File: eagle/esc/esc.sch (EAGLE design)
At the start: 88 parts, among them IC1 DRV8305NPHPR, IC2 STM32L431CCT6LQFP48, IC3 FT232RL, J2 ARM10-CON, T1 CSD17573Q5B, T2 CSD17573Q5B, T3 CSD17573Q5B, T4 CSD17573Q5B, T5 CSD17573Q5B, T6 CSD17573Q5B, U1 LD1117S50TR1, U2 MIC5319-3.3YD5-TR, X1 C-GRID-02-15-19, X2 MINI-USB-32005-301

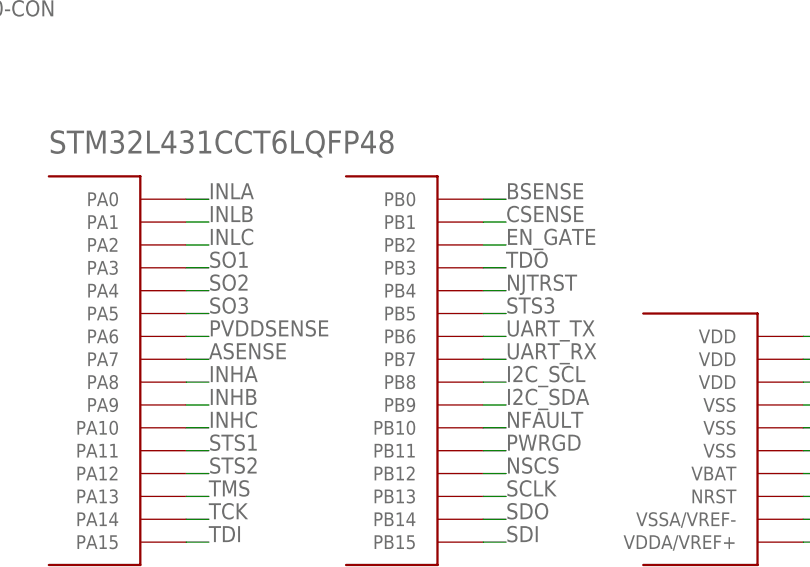
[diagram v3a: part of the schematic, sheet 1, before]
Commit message: updated pin mappings - changed a bunch for better placements
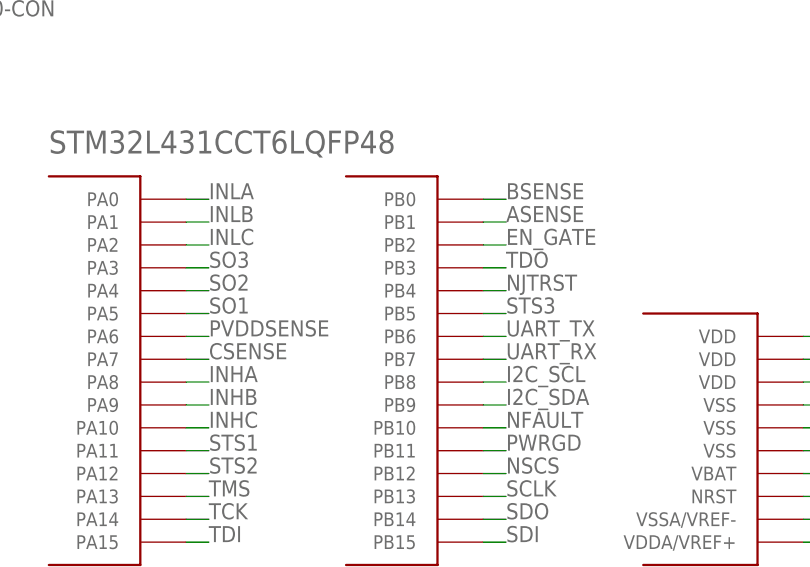
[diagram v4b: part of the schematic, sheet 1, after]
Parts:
- C2, C5, C8: device resistor:C-EUC0603 -> resistor:C-EUC0402
- R1, R2, R4, R5, R7, R8: device resistor:R-US_R0603 -> resistor:R-US_R0402
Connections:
- net ASENSE: now also IC2.PB1; no longer IC2.PA7
- net CSENSE: now also IC2.PA7; no longer IC2.PB1
- net SO1: now also IC2.PA5; no longer IC2.PA3
- net SO3: now also IC2.PA3; no longer IC2.PA5
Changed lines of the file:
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@@
 <part name="IC2" library="qc_esc" deviceset="STM32L431CCT6" device="LQFP48" package3d_urn="urn:adsk.eagle:package:16300078/1"/>
 <part name="C1" library="resistor" library_urn="urn:adsk.eagle:library:348" deviceset="C-EU" device="C0603" package3d_urn="urn:adsk.eagle:package:23616/2" value="1 uF"/>
-<part name="C2" library="resistor" library_urn="urn:adsk.eagle:library:348" deviceset="C-EU" device="C0603" package3d_urn="urn:adsk.eagle:package:23616/2" value="0.1 uF"/>
+<part name="C2" library="resistor" library_urn="urn:adsk.eagle:library:348" deviceset="C-EU" device="C0402" package3d_urn="urn:adsk.eagle:package:23626/2" value="0.1 uF"/>
 <part name="D1" library="qc_esc" deviceset="STPS2L30A" device="SMA" package3d_urn="urn:adsk.eagle:package:18881571/1"/>
-<part name="R1" library="resistor" library_urn="urn:adsk.eagle:library:348" deviceset="R-US_" device="R0603" package3d_urn="urn:adsk.eagle:package:23555/3" value="34.8k"/>
-<part name="R2" library="resistor" library_urn="urn:adsk.eagle:library:348" deviceset="R-US_" device="R0603" package3d_urn="urn:adsk.eagle:package:23555/3" value="4.99k"/>
+<part name="R1" library="resistor" library_urn="urn:adsk.eagle:library:348" deviceset="R-US_" device="R0402" package3d_urn="urn:adsk.eagle:package:26058/2" value="34.8k"/>
+<part name="R2" library="resistor" library_urn="urn:adsk.eagle:library:348" deviceset="R-US_" device="R0402" package3d_urn="urn:adsk.eagle:package:26058/2" value="4.99k"/>
 <part name="VDD1" library="supply1" library_urn="urn:adsk.eagle:library:371" deviceset="VDD" device=""/>
 <part name="SUPPLY1" library="supply2" library_urn="urn:adsk.eagle:library:372" deviceset="GND" device=""/>
@@
 <part name="T4" library="qc_esc" deviceset="CSD17573Q5B" device=""/>
 <part name="C4" library="resistor" library_urn="urn:adsk.eagle:library:348" deviceset="C-EU" device="C0603" package3d_urn="urn:adsk.eagle:package:23616/2" value="1 uF"/>
-<part name="C5" library="resistor" library_urn="urn:adsk.eagle:library:348" deviceset="C-EU" device="C0603" package3d_urn="urn:adsk.eagle:package:23616/2" value="0.1 uF"/>
+<part name="C5" library="resistor" library_urn="urn:adsk.eagle:library:348" deviceset="C-EU" device="C0402" package3d_urn="urn:adsk.eagle:package:23626/2" value="0.1 uF"/>
 <part name="D2" library="qc_esc" deviceset="STPS2L30A" device="SMA" package3d_urn="urn:adsk.eagle:package:18881571/1"/>
-<part name="R4" library="resistor" library_urn="urn:adsk.eagle:library:348" deviceset="R-US_" device="R0603" package3d_urn="urn:adsk.eagle:package:23555/3" value="34.8k"/>
-<part name="R5" library="resistor" library_urn="urn:adsk.eagle:library:348" deviceset="R-US_" device="R0603" package3d_urn="urn:adsk.eagle:package:23555/3" value="4.99k"/>
+<part name="R4" library="resistor" library_urn="urn:adsk.eagle:library:348" deviceset="R-US_" device="R0402" package3d_urn="urn:adsk.eagle:package:26058/2" value="34.8k"/>
+<part name="R5" library="resistor" library_urn="urn:adsk.eagle:library:348" deviceset="R-US_" device="R0402" package3d_urn="urn:adsk.eagle:package:26058/2" value="4.99k"/>
 <part name="VDD2" library="supply1" library_urn="urn:adsk.eagle:library:371" deviceset="VDD" device=""/>
 <part name="SUPPLY4" library="supply2" library_urn="urn:adsk.eagle:library:372" deviceset="GND" device=""/>
@@
 <part name="T6" library="qc_esc" deviceset="CSD17573Q5B" device=""/>
 <part name="C7" library="resistor" library_urn="urn:adsk.eagle:library:348" deviceset="C-EU" device="C0603" package3d_urn="urn:adsk.eagle:package:23616/2" value="1 uF"/>
-<part name="C8" library="resistor" library_urn="urn:adsk.eagle:library:348" deviceset="C-EU" device="C0603" package3d_urn="urn:adsk.eagle:package:23616/2" value="0.1 uF"/>
+<part name="C8" library="resistor" library_urn="urn:adsk.eagle:library:348" deviceset="C-EU" device="C0402" package3d_urn="urn:adsk.eagle:package:23626/2" value="0.1 uF"/>
 <part name="D3" library="qc_esc" deviceset="STPS2L30A" device="SMA" package3d_urn="urn:adsk.eagle:package:18881571/1"/>
-<part name="R7" library="resistor" library_urn="urn:adsk.eagle:library:348" deviceset="R-US_" device="R0603" package3d_urn="urn:adsk.eagle:package:23555/3" value="34.8k"/>
-<part name="R8" library="resistor" library_urn="urn:adsk.eagle:library:348" deviceset="R-US_" device="R0603" package3d_urn="urn:adsk.eagle:package:23555/3" value="4.99k"/>
+<part name="R7" library="resistor" library_urn="urn:adsk.eagle:library:348" deviceset="R-US_" device="R0402" package3d_urn="urn:adsk.eagle:package:26058/2" value="34.8k"/>
+<part name="R8" library="resistor" library_urn="urn:adsk.eagle:library:348" deviceset="R-US_" device="R0402" package3d_urn="urn:adsk.eagle:package:26058/2" value="4.99k"/>
 <part name="VDD3" library="supply1" library_urn="urn:adsk.eagle:library:371" deviceset="VDD" device=""/>
 <part name="SUPPLY7" library="supply2" library_urn="urn:adsk.eagle:library:372" deviceset="GND" device=""/>
@@
 <net name="SO1" class="0">
 <segment>
-<pinref part="IC2" gate="G$1" pin="PA3"/>
-<wire x1="66.04" y1="91.44" x2="68.58" y2="91.44" width="0.1524" layer="91"/>
-<label x="68.58" y="91.44" size="1.778" layer="95"/>
+<pinref part="IC2" gate="G$1" pin="PA5"/>
+<wire x1="66.04" y1="86.36" x2="68.58" y2="86.36" width="0.1524" layer="91"/>
+<label x="68.58" y="86.36" size="1.778" layer="95"/>
 </segment>
 </net>
@@
 </segment>
 </net>
-<net name="SO3" class="0">
-<segment>
-<pinref part="IC2" gate="G$1" pin="PA5"/>
-<wire x1="66.04" y1="86.36" x2="68.58" y2="86.36" width="0.1524" layer="91"/>
-<label x="68.58" y="86.36" size="1.778" layer="95"/>
-</segment>
-</net>
 <net name="PVDDSENSE" class="0">
 <segment>
@@
 </segment>
 </net>
-<net name="ASENSE" class="0">
+<net name="INHA" class="0">
+<segment>
+<pinref part="IC2" gate="G$1" pin="PA8"/>
+<wire x1="66.04" y1="78.74" x2="68.58" y2="78.74" width="0.1524" layer="91"/>
+<label x="68.58" y="78.74" size="1.778" layer="95"/>
+</segment>
+</net>
+<net name="INHB" class="0">
+<segment>
+<pinref part="IC2" gate="G$1" pin="PA9"/>
+<wire x1="66.04" y1="76.2" x2="68.58" y2="76.2" width="0.1524" layer="91"/>
+<label x="68.58" y="76.2" size="1.778" layer="95"/>
+</segment>
+</net>
+<net name="INHC" class="0">
+<segment>
+<pinref part="IC2" gate="G$1" pin="PA10"/>
+<wire x1="66.04" y1="73.66" x2="68.58" y2="73.66" width="0.1524" layer="91"/>
+<label x="68.58" y="73.66" size="1.778" layer="95"/>
+</segment>
+</net>
+<net name="BSENSE" class="0">
+<segment>
+<pinref part="IC2" gate="G$1" pin="PB0"/>
+<wire x1="99.06" y1="99.06" x2="101.6" y2="99.06" width="0.1524" layer="91"/>
+<label x="101.6" y="99.06" size="1.778" layer="95"/>
+</segment>
+</net>
+<net name="CSENSE" class="0">
 <segment>
 <pinref part="IC2" gate="G$1" pin="PA7"/>
 <wire x1="66.04" y1="81.28" x2="68.58" y2="81.28" width="0.1524" layer="91"/>
 <label x="68.58" y="81.28" size="1.778" layer="95"/>
-</segment>
-</net>
-<net name="INHA" class="0">
-<segment>
-<pinref part="IC2" gate="G$1" pin="PA8"/>
-<wire x1="66.04" y1="78.74" x2="68.58" y2="78.74" width="0.1524" layer="91"/>
-<label x="68.58" y="78.74" size="1.778" layer="95"/>
-</segment>
-</net>
-<net name="INHB" class="0">
-<segment>
-<pinref part="IC2" gate="G$1" pin="PA9"/>
-<wire x1="66.04" y1="76.2" x2="68.58" y2="76.2" width="0.1524" layer="91"/>
-<label x="68.58" y="76.2" size="1.778" layer="95"/>
-</segment>
-</net>
-<net name="INHC" class="0">
-<segment>
-<pinref part="IC2" gate="G$1" pin="PA10"/>
-<wire x1="66.04" y1="73.66" x2="68.58" y2="73.66" width="0.1524" layer="91"/>
-<label x="68.58" y="73.66" size="1.778" layer="95"/>
-</segment>
-</net>
-<net name="BSENSE" class="0">
-<segment>
-<pinref part="IC2" gate="G$1" pin="PB0"/>
-<wire x1="99.06" y1="99.06" x2="101.6" y2="99.06" width="0.1524" layer="91"/>
-<label x="101.6" y="99.06" size="1.778" layer="95"/>
-</segment>
-</net>
-<net name="CSENSE" class="0">
-<segment>
-<pinref part="IC2" gate="G$1" pin="PB1"/>
-<wire x1="99.06" y1="96.52" x2="101.6" y2="96.52" width="0.1524" layer="91"/>
-<label x="101.6" y="96.52" size="1.778" layer="95"/>
 </segment>
 </net>
@@
 </segment>
 </net>
+<net name="SO3" class="0">
+<segment>
+<pinref part="IC2" gate="G$1" pin="PA3"/>
+<wire x1="66.04" y1="91.44" x2="68.58" y2="91.44" width="0.1524" layer="91"/>
+<label x="68.58" y="91.44" size="1.778" layer="95"/>
+</segment>
+</net>
+<net name="ASENSE" class="0">
+<segment>
+<pinref part="IC2" gate="G$1" pin="PB1"/>
+<wire x1="99.06" y1="96.52" x2="101.6" y2="96.52" width="0.1524" layer="91"/>
+<label x="101.6" y="96.52" size="1.778" layer="95"/>
+</segment>
+</net>
